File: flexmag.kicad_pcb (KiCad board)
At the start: 2 copper layers, 181.7 x 16 mm, 7 parts, among them J1 Conn_01x06_Male, J2 Conn_01x06_Male, U1 AS5600-ASOM

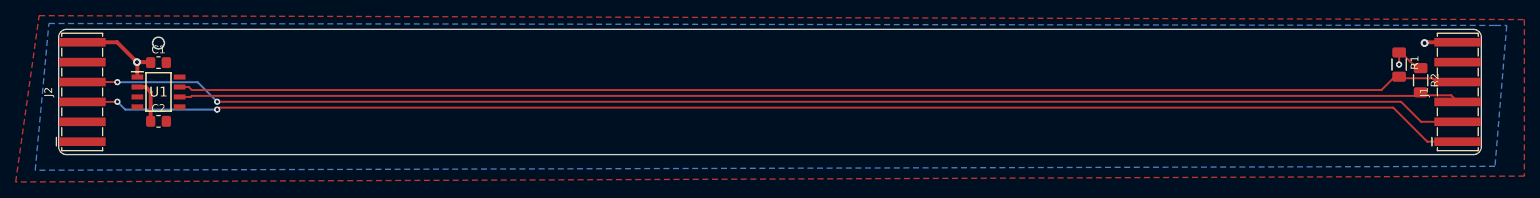
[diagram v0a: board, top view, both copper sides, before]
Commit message: now as sigle sided PCB
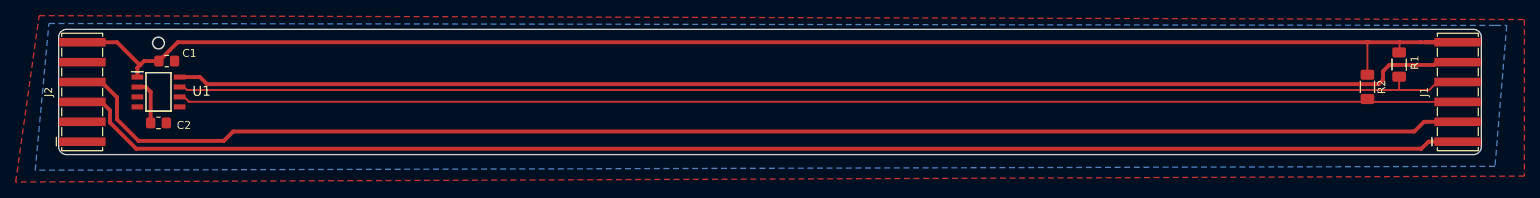
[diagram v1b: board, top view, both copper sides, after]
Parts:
- moved R2 6.85 mm to (223.7, 47.6)
- moved C1 1.07 mm to (70.3, 44.3)
- moved C2 0.20 mm to (69.2, 52.2)
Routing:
- net +5V: track 21.0 -> 194.2 mm, vias 3 -> 0
- net GND: track 0.00 -> 165.5 mm
- net Net-(J1-Pad2): track 177.9 -> 181.5 mm, vias 2 -> 0
- net Net-(J1-Pad1): track 178.1 -> 179.5 mm, vias 2 -> 0
- net Net-(J1-Pad4): track 164.3 -> 165.6 mm

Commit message: Perfect is the enemy of done
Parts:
- added REF**: TestPoint_Pad_1.0x1.0mm, TestPoint:TestPoint_Pad_1.0x1.0mm, F.Cu at (74.5, 50.9)
- added REF**: jmp, TestPoint:jmp, F.Cu at (217.1, 47.4)
- added REF**: TestPoint_Pad_1.0x1.0mm, TestPoint:TestPoint_Pad_1.0x1.0mm, F.Cu at (64.3, 46.6)
- moved C1 4.67 mm to (65.7, 43.3), turned to 90 degrees
- moved R1 2.75 mm to (225.6, 46.5)
- moved R2 2.19 mm to (221.5, 48.0)
- moved J1 2.16 mm to (233.1, 48.2)
- renumbered U1 to AS5600
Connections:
- J1 pad 5: GND -> +5V
- J1 pad 6: +5V -> GND
- J2 pad 5: GND -> +5V
- J2 pad 6: +5V -> GND
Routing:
- net GND: track 165.5 -> 29.2 mm
- net +5V: track 194.2 -> 178.3 mm
- net unconnected-(U1-Pad3): track 0.00 -> 3.87 mm
- net unconnected-(U1-Pad5): track 0.00 -> 2.87 mm
- net Net-(J1-Pad2): track 181.5 -> 179.4 mm
- net Net-(J1-Pad1): track 179.5 -> 177.7 mm
- net Net-(J1-Pad4): track 165.6 -> 164.0 mm
- net Net-(J1-Pad3): track 163.9 -> 162.5 mm
- removed copper zone on B.Cu, net +5V
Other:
- board size 181.7 x 16 mm -> 180 x 16 mm
- board text added: "PGO"
- board text added: "PWM"
